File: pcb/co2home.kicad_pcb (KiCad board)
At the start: 2 copper layers, 40 x 70 mm, 20 parts, among them J1 eflashy32, J2 MH-Z19 L, J3 USBC, J4 MH-Z19 R, J5 JST-PH, SW1 RESET, U1 ESP32-C3-MINI-1, U4 AMS1117-3.3

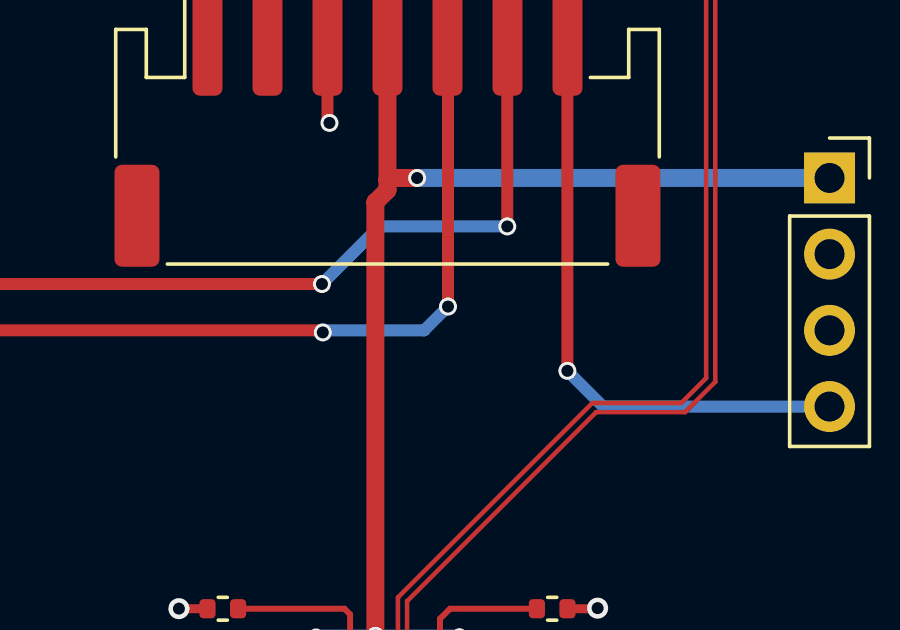
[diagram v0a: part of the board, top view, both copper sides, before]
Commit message: silkscreen for pins
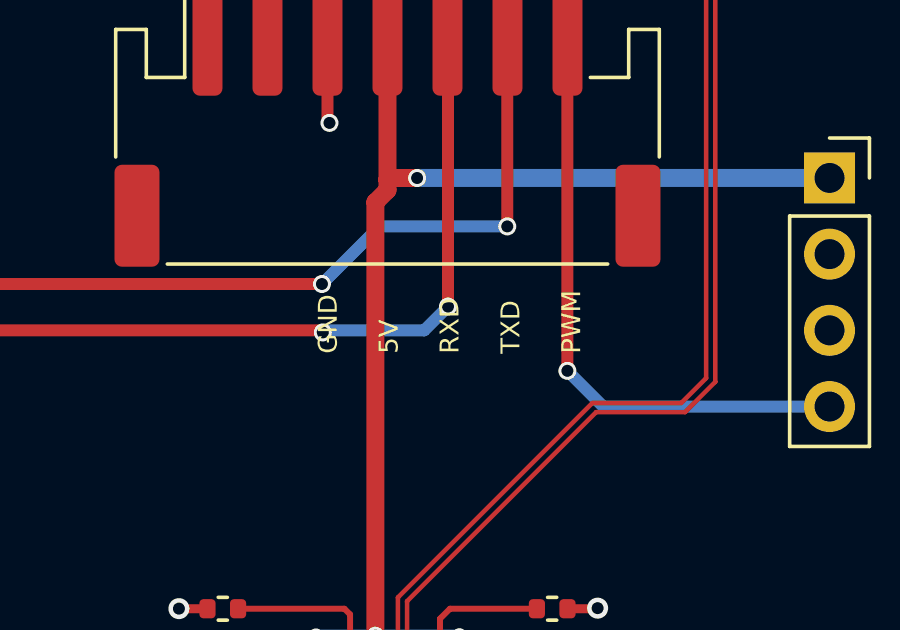
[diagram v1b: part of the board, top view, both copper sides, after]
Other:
- board text added: "GND 5V RXD TXD PWM"
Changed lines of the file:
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@@
     (effects (font (size 1 1) (thickness 0.15)))
+  )
+  (gr_text "GND\n\n5V\n\nRXD\n\nTXD\n\nPWM" (at 141.425 86.2 90) (layer "F.SilkS")
+    (effects (font (size 0.63 0.63) (thickness 0.12)) (justify left bottom))
   )
   (gr_text "Thermal break" (at 123.925 66.7) (layer "Cmts.User")

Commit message: PN for headers
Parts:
- moved J3 0.10 mm to (134.9, 101.1)
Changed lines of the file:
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@@
     (descr "Through hole straight socket strip, 1x05, 2.54mm pitch, single row (from Kicad 4.0.7), script generated")
     (tags "Through hole socket strip THT 1x05 2.54mm single row")
+    (property "LCSC" "C50950")
     (property "Sheetfile" "co2home.kicad_sch")
     (property "Sheetname" "")
@@
   )
   (footprint "Connector_USB:USB_C_Receptacle_GCT_USB4105-xx-A_16P_TopMnt_Horizontal" (layer "F.Cu")
-    (at 134.925 101.2)
+    (at 134.925 101.1)
     (descr "USB 2.0 Type C Receptacle, GCT, 16P, top mounted, horizontal, 5A: https://gct.co/files/drawings/usb4105.pdf")
     (tags "USB C Type-C Receptacle SMD USB 2.0 16P 16C USB4105-15-A USB4105-15-A-060 USB4105-15-A-120 USB4105-GF-A USB4105-GF-A-060 USB4105-GF-A-120")
@@
     (descr "Through hole straight socket strip, 1x04, 2.54mm pitch, single row (from Kicad 4.0.7), script generated")
     (tags "Through hole socket strip THT 1x04 2.54mm single row")
-    (property "Sheetfile" "co2home.kicad_sch")
-    (property "Sheetname" "")
+    (property "LCSC" "C2718488")
+    (property "Sheetfile" "co2home.kicad_sch")
+    (property "Sheetname" "")
